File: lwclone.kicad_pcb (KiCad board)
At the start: 2 copper layers, 30 x 14 mm, 13 parts, among them U1 ATtiny85-20PU

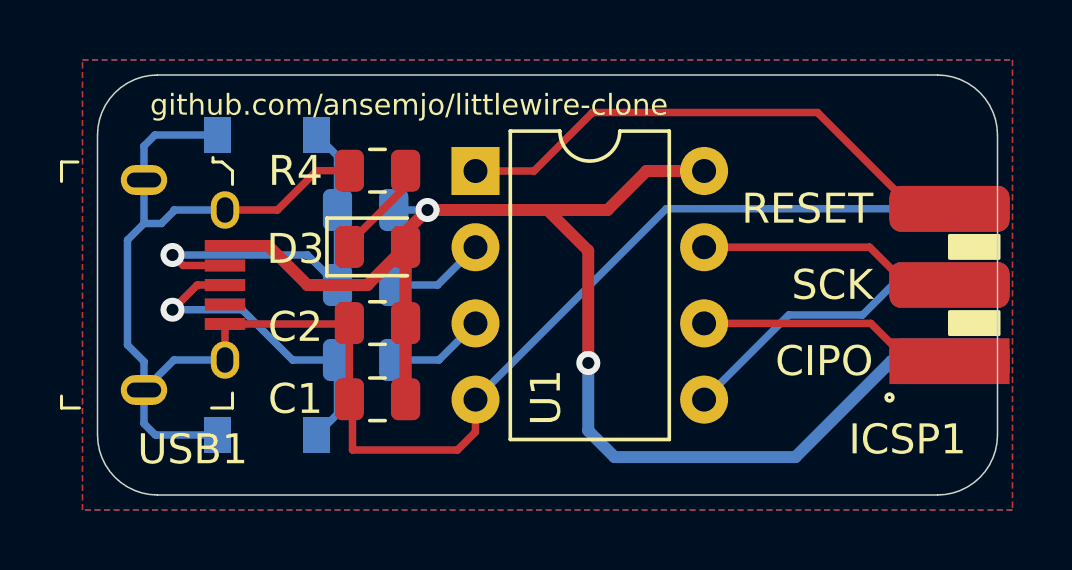
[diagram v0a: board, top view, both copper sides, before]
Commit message: copy all used symbols to local lwclone.lib
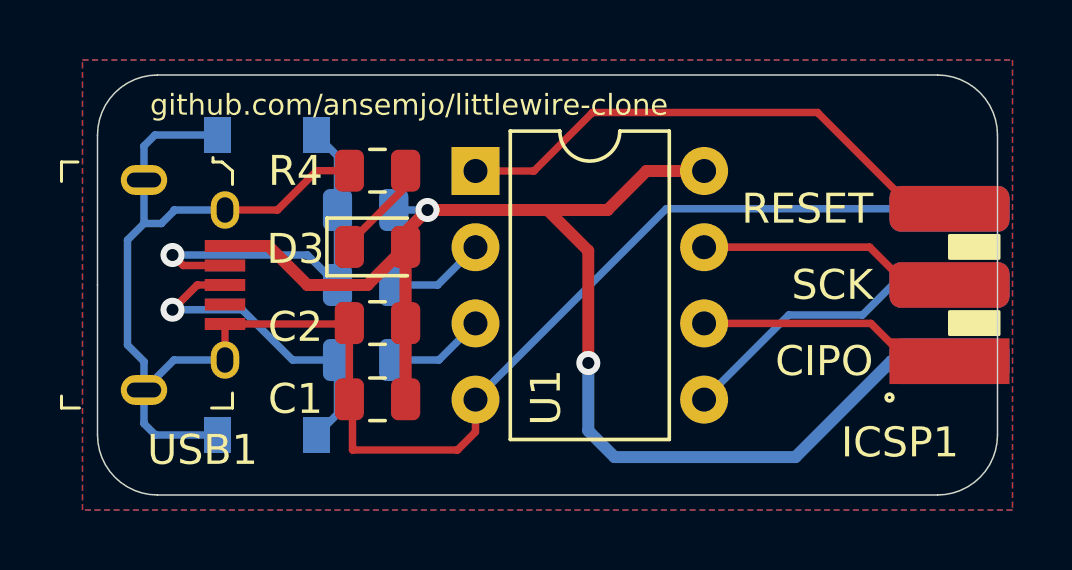
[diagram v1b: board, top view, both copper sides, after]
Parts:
- USB1: footprint digikey-footprints:USB_Micro_B_Female_10118194-0001LF -> lwclone:USB_Micro_B_Female_10118194-0001LF
